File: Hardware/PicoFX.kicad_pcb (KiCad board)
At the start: 4 copper layers, 59 x 95 mm, 105 parts, among them J1 RPI_ADC, J2 RP_GPIO, U1 AMS1117-5.0, U2 AMS1117-3.3, U3 MCP6002-xSN, U4 MCP6002-xSN, U5 CS4272, X1 PEDAL_COMBO_TOP

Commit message: Output files
Minor changes to the board and schematic.
Updated the output files.
Added a 3D model of the complete board.
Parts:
- removed the REF** at (150.0, 100.0)
- added FID1: Fiducial, Fiducial:Fiducial_0.75mm_Mask1.5mm, B.Cu at (177.4, 58.0)
- added FID2: Fiducial, Fiducial:Fiducial_0.75mm_Mask1.5mm, B.Cu at (122.6, 58.0)
- added FID3: Fiducial, Fiducial:Fiducial_0.75mm_Mask1.5mm, B.Cu at (177.4, 91.4)
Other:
- board text added: "PD 05/26"
- board text removed: "PD 04/26"

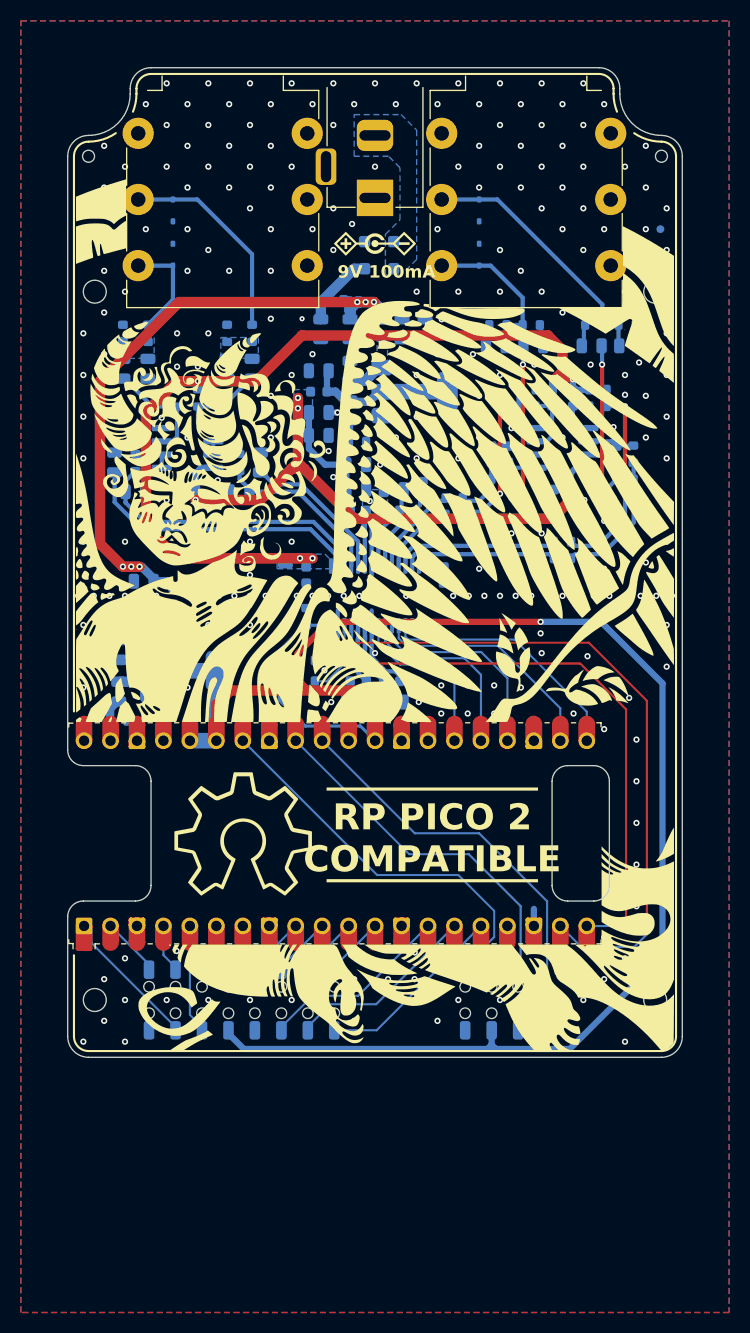
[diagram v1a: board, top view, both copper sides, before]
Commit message: Assembly review
Performed a full review of the schematic and layout.
Minor changes to the schematic and layout.
Updated output files.
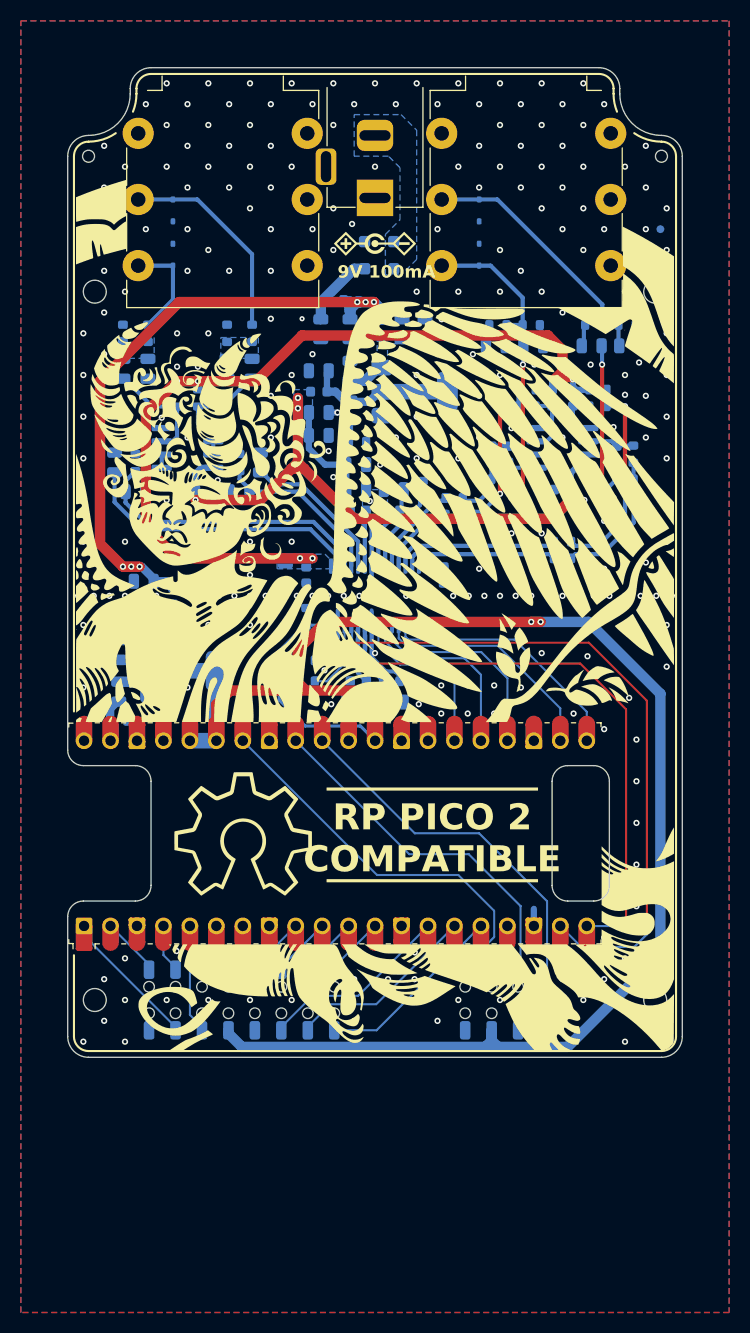
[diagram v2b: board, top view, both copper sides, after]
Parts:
- R29, R30: value 47K -> 2.2K
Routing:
- net +3V3D: track 171.8 -> 175.6 mm, vias 4 -> 5
- net GND: vias 283 -> 282

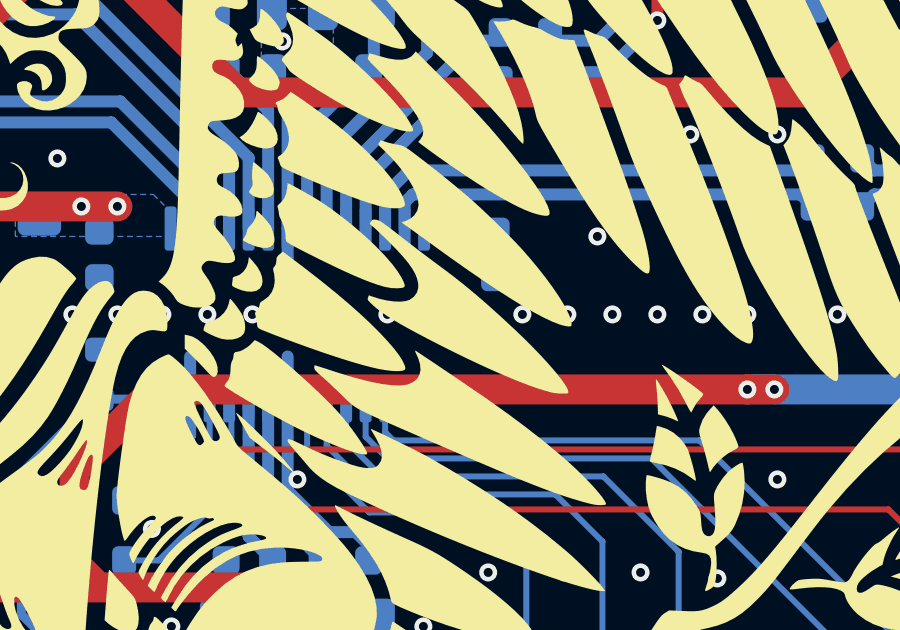
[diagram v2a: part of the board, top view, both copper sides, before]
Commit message: Initial software release
Added an initial sine generator application.
Only the I2S output is working via PIO.
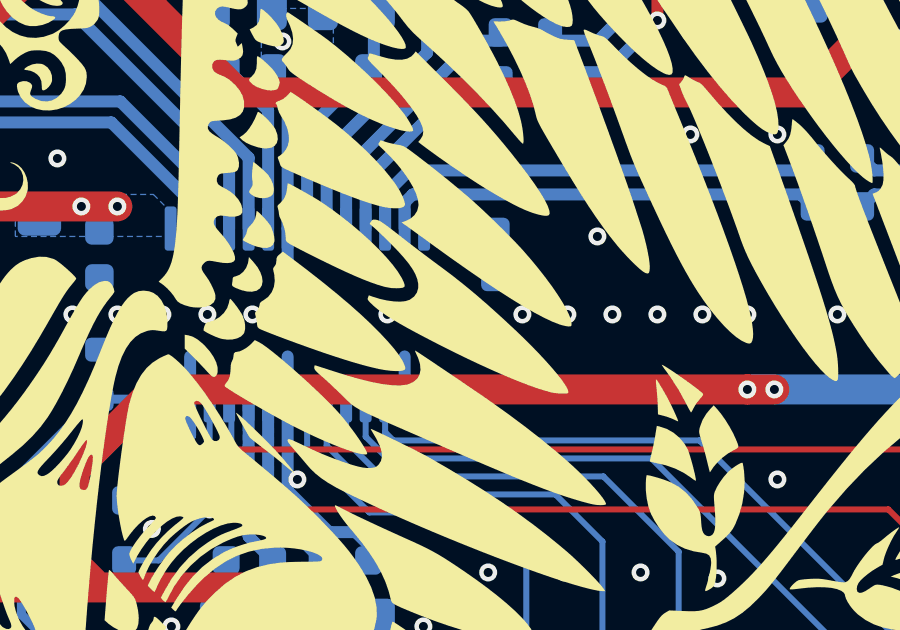
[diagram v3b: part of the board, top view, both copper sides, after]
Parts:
- R2: value 100 -> 10
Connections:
- U5 pad 2: unconnected-(U5-XTI-Pad2) -> GND
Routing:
- net GND: track 24.0 -> 25.5 mm
